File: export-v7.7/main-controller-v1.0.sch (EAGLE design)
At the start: 33 parts, among them IC21 TCA9539PW, J1 PJ-3200-STEREO-JACK, M1 TEENSY4.1-BARE

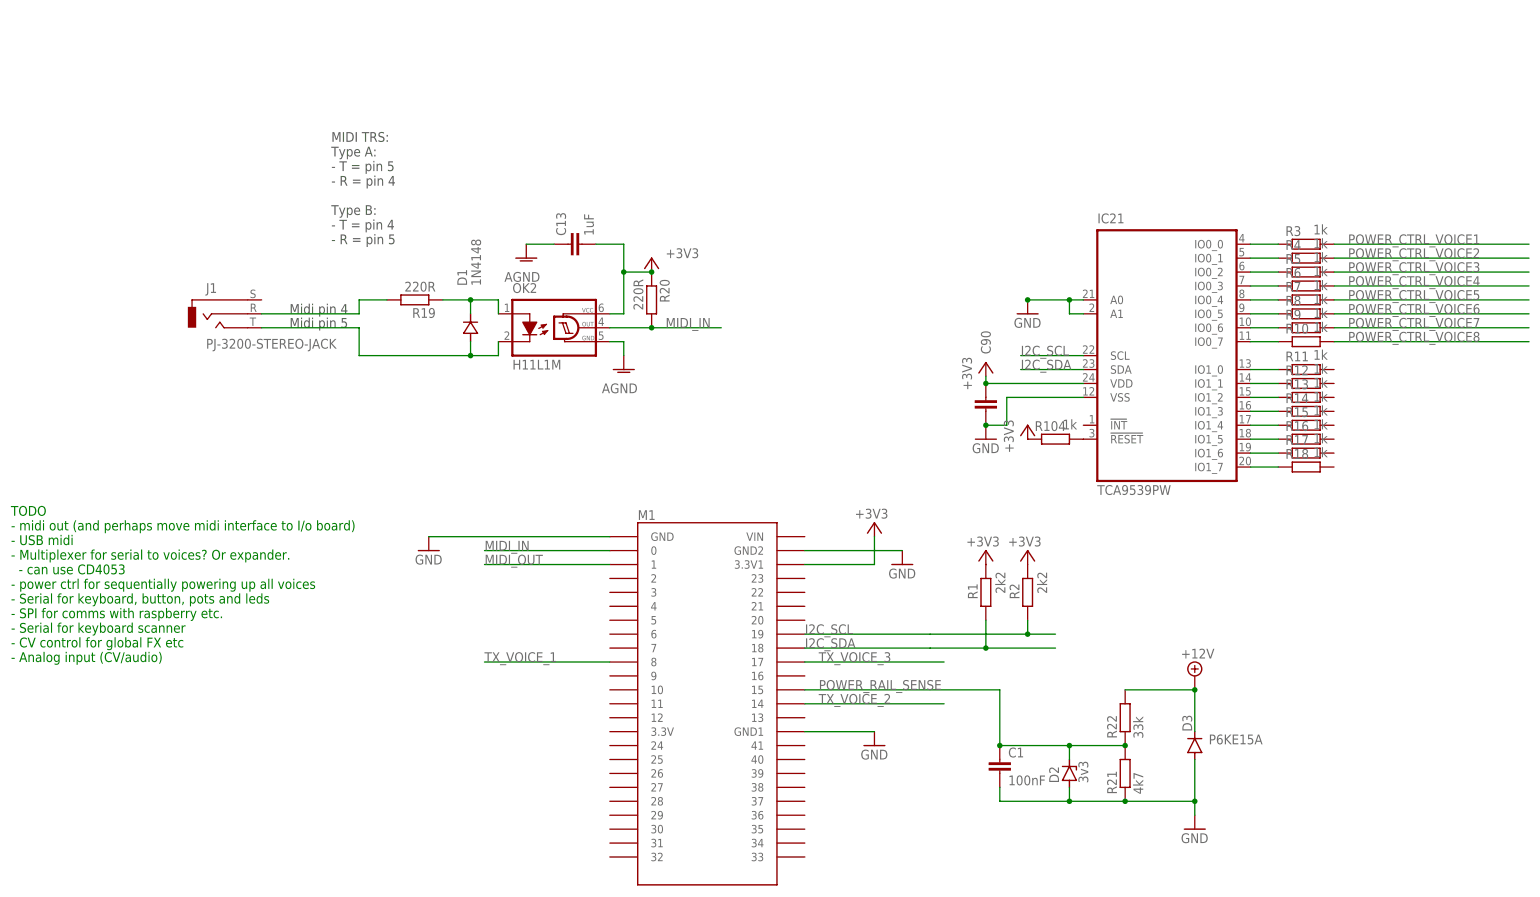
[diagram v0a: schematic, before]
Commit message: USB Power supply into
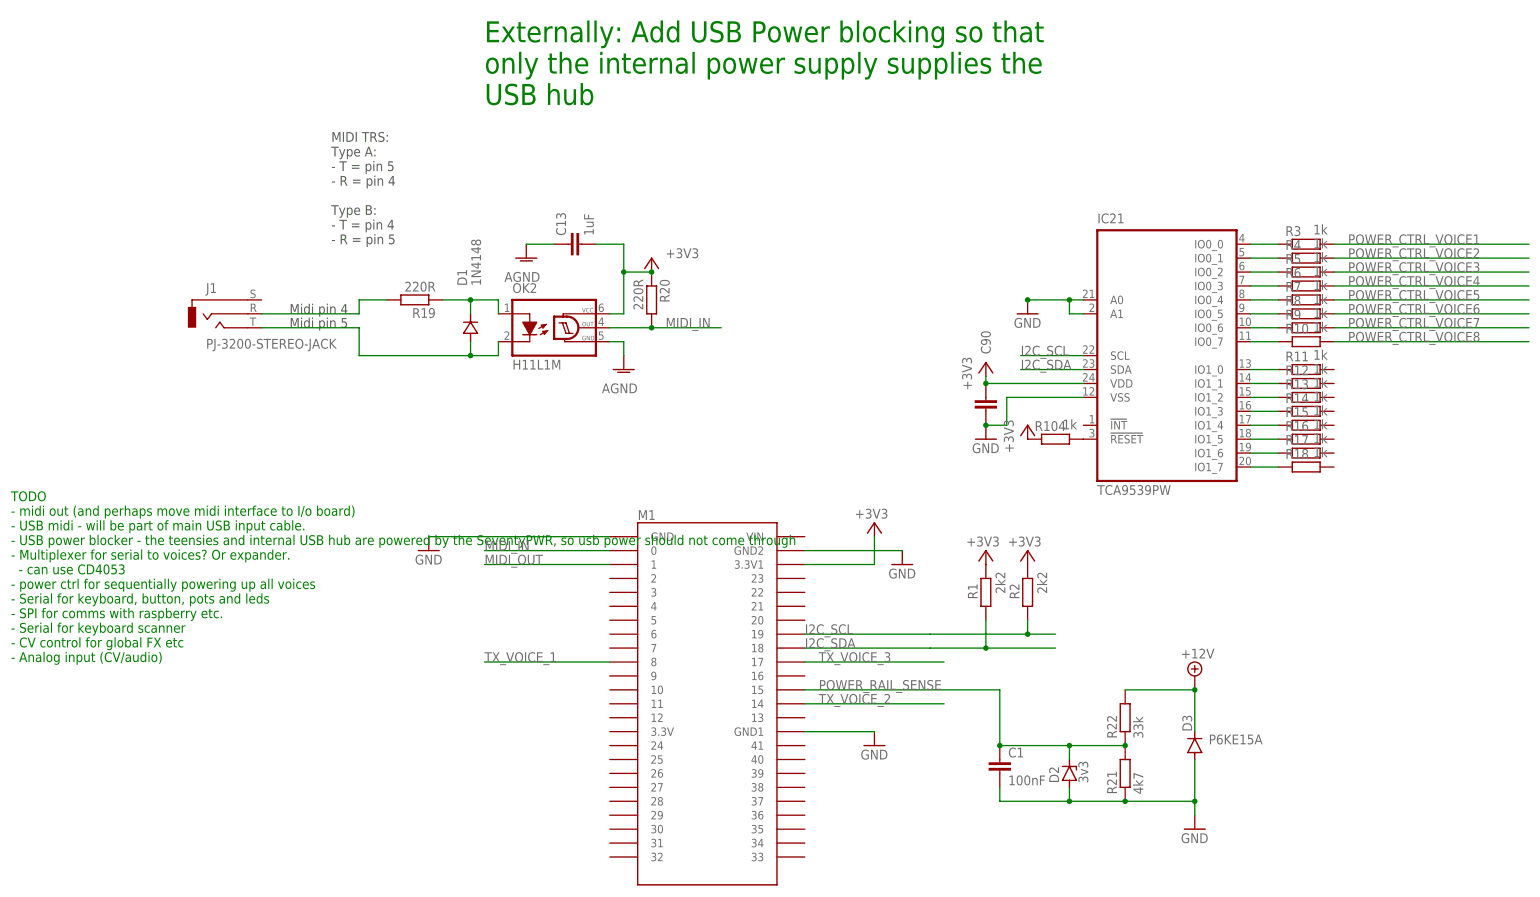
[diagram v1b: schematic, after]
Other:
- note added: "Externally: Add USB Power blocking so that only the internal power supply supplies the USB hub"
- note added: "TODO - midi out (and perhaps move midi interface to I/o board) - USB midi - will be part of main USB input cable. - USB power blocker - the teensies and internal USB hub are powered by the SeventyPWR, so usb power should not come through - Multiplexer for serial to voices? Or expander. - can use CD4053 - power ctrl for sequentially powering up all voices - Serial for keyboard, button, pots and le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"
- note removed: "TODO - midi out (and perhaps move midi interface to I/o board) - USB midi - Multiplexer for serial to voices? Or expander. - can use CD4053 - power ctrl for sequentially powering up all voices - Serial for keyboard, button, pots and leds - SPI for comms with raspberry etc. - Serial for keyboard scanner - CV control for global FX etc - Analog input (CV/audio)"
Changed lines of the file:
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@@
 <text x="-50.8" y="5.08" size="1.778" layer="91">TODO
 - midi out (and perhaps move midi interface to I/o board)
-- USB midi
+- USB midi - will be part of main USB input cable.
+- USB power blocker - the teensies and internal USB hub are powered by the SeventyPWR, so usb power should not come through
 - Multiplexer for serial to voices? Or expander.
   - can use CD4053
@@
 - CV control for global FX etc
 - Analog input (CV/audio)</text>
+<text x="35.56" y="106.68" size="3.81" layer="91">Externally: Add USB Power blocking so that
+only the internal power supply supplies the
+USB hub</text>
 </plain>
 <instances>
